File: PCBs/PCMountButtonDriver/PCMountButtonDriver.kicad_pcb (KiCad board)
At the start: 2 copper layers, 55.9 x 21.5 mm, 12 parts, among them U1 74HC164

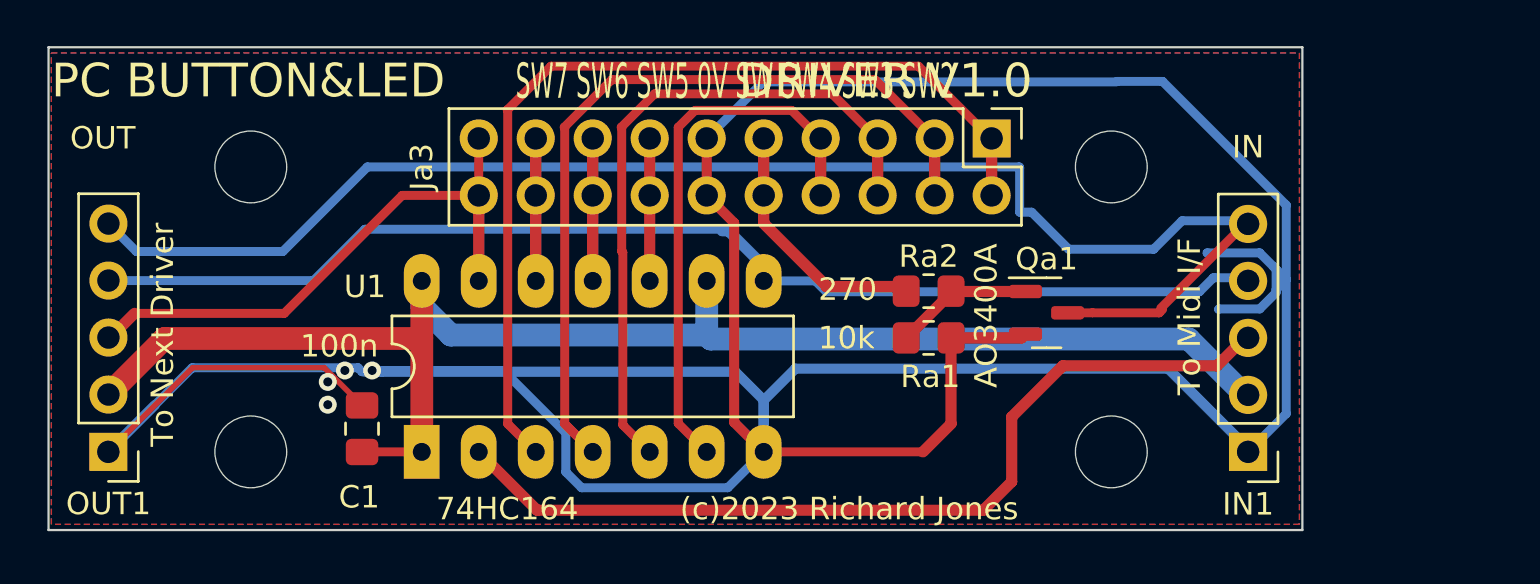
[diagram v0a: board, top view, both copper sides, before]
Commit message: V1.1 PCB updates after initial testing 1. Share data out line between LCD, 7 Segment and button scan to yield spare io lines for    control of WS8212 LEDs for music stand lamp 2. Replace level shifting FET on Button Driver PCBs by resistor 3. Generate combined ks61,button driver & button mount prototype PCB for economic testing with JLC PCB
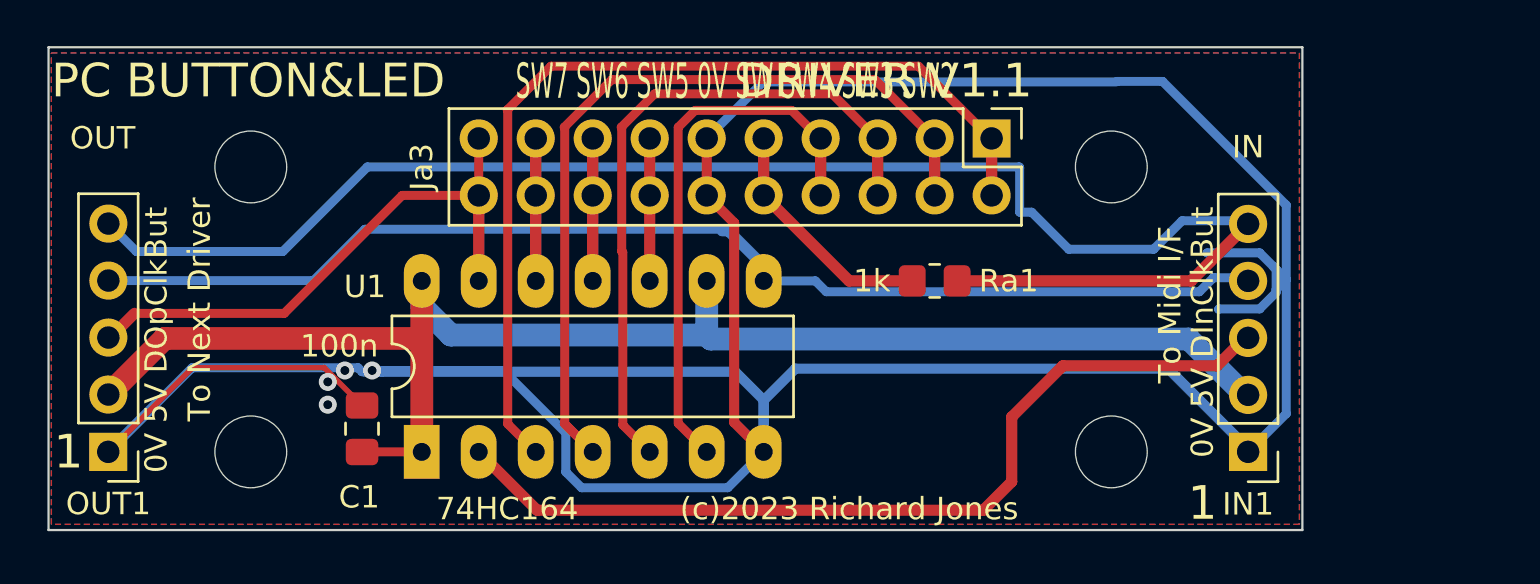
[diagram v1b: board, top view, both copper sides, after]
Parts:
- removed Qa1: AO3400A, Package_TO_SOT_SMD:SOT-23
- removed Ra2: 270, Resistor_SMD:R_0805_2012Metric_Pad1.20x1.40mm_HandSolder
- Ra1: value 10k -> 1k
- moved Ra1 2.55 mm to (172.7, 104.1)
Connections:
- IN1 pad 5: Net-(OUT1-Pad5) -> Net-(IN1-Pad5)
- OUT1 pad 5: Net-(OUT1-Pad5) -> Net-(IN1-Pad5)
- Ra1 pad 1: /0.V -> Net-(IN1-Pad5)
- Ra1 pad 2: Net-(Qa1-Pad1) -> /.SW
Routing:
- net Net-(IN1-Pad5): track 0.00 -> 70.1 mm
- net Net-(OUT1-Pad5): track 65.9 -> 0.00 mm
- net /0.V: track 175.4 -> 159.1 mm
- net Net-(Qa1-Pad1): track 6.24 -> 0.00 mm
- net /.SW: track 11.4 -> 10.7 mm
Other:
- board text added: "0V 5V DInClkBut"
- board text added: "0V 5V DOpClkBut"
- board text added: "1"
- board text added: "PC BUTTON & LED DRIVER V1.1"
- board text added: "PC BUTTON&LED DRIVER V1.1"
- board text added: "SW8 SW7 SW6 SW5 SW 0V SW4 SW3 SW2 SW1"
- board text removed: "PC BUTTON&LED DRIVER V1.0"
